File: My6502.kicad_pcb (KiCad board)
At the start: 2 copper layers, 99.7 x 99.7 mm, 38 parts, among them J1 ~NMI, J3 Power 5V, J4 Expansion Bus, J5 Port A, J6 Port B, SW1 RESET, U1 6502, U2 ROM 28C256, U3 RAM 62256, U4 74HCT00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

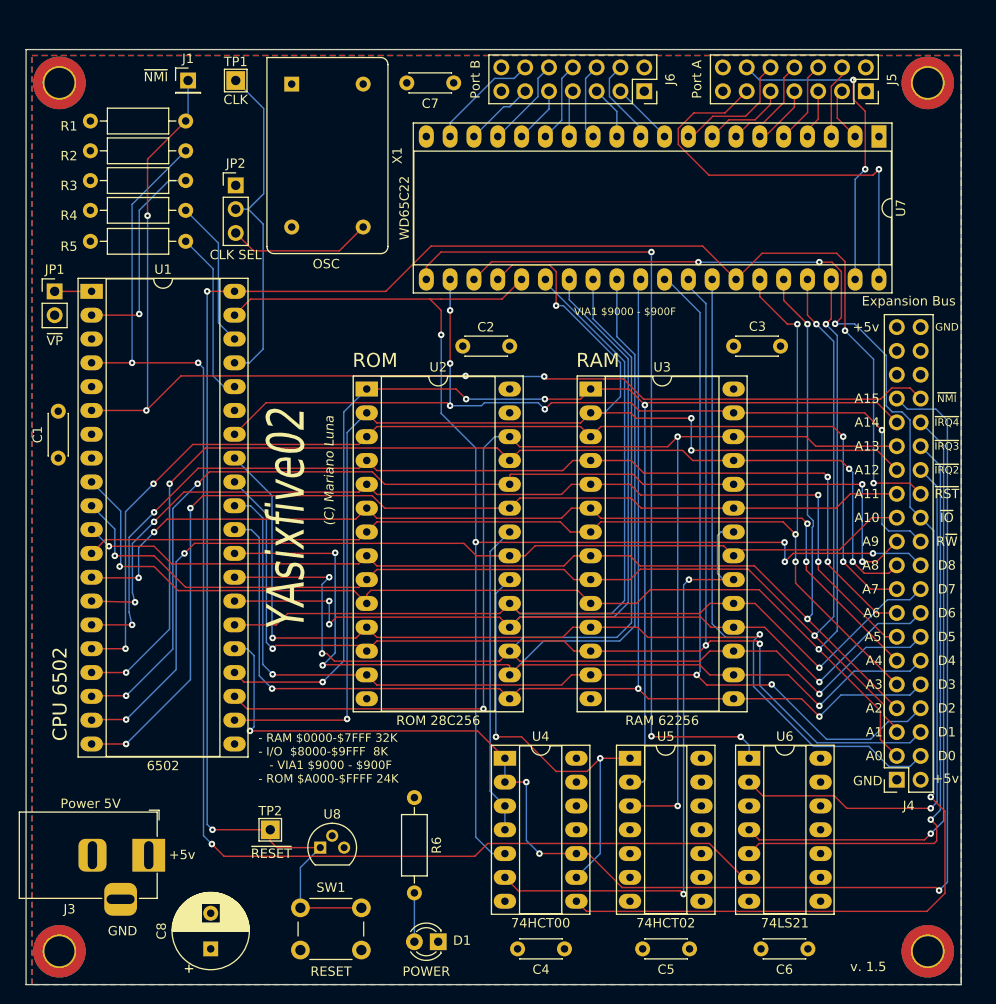
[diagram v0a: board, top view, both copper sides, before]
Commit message: Gerber file deleted had errors. New Schematic with power leads and GND Test
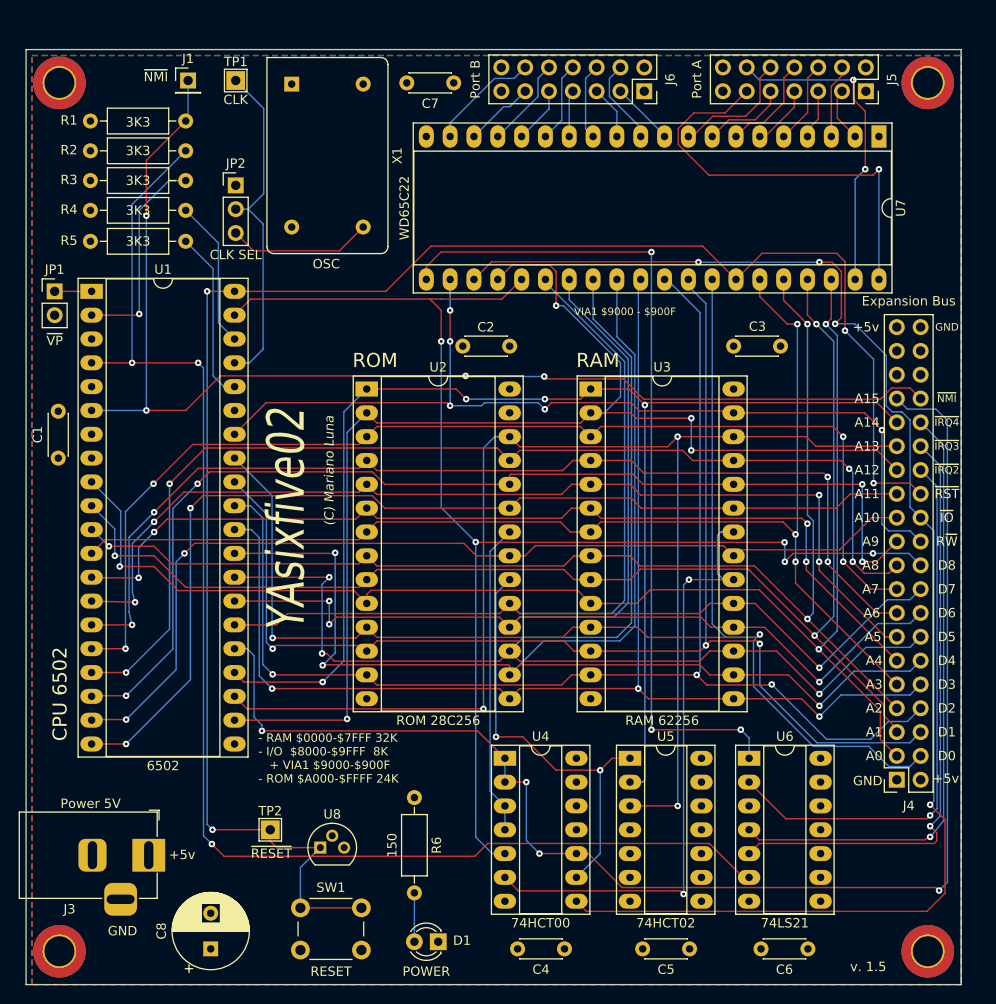
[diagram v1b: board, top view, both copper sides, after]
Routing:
- net ~ROM_CS: track 47.5 -> 46.2 mm
- net ~VIA2_IRQ: track 57.6 -> 58.9 mm
- net a15: track 153.1 -> 152.0 mm
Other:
- board text added: "- RAM $0000-$7FFF 32K - I/O $8000-$9FFF 8K + VIA1 $9000-$900F - ROM $A000-$FFFF 24K"
- board text removed: "- RAM $0000-$7FFF 32K - I/O $8000-$9FFF 8K - VIA1 $9000 - $900F - ROM $A000-$FFFF 24K"

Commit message: YAsicfive02 1.5 final version - Gerber file done
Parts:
- added J2: Aux 5VDC, Connector_PinHeader_2.54mm:PinHeader_1x03_P2.54mm_Vertical, F.Cu at (41.1, 146.2)
- added J7: GND, Connector_PinHeader_2.54mm:PinHeader_1x01_P2.54mm_Vertical, F.Cu at (122.2, 144.0)
- U1: value 6502 -> CPU 6502
- moved C8 5.80 mm to (53.8, 141.1), turned to 180 degrees
- moved J3 0.81 mm to (44.2, 135.3)
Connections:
- J3 pad 3: GND -> Net-(J2-Pad1)
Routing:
- net Net-(J2-Pad1): track 0.00 -> 11.9 mm

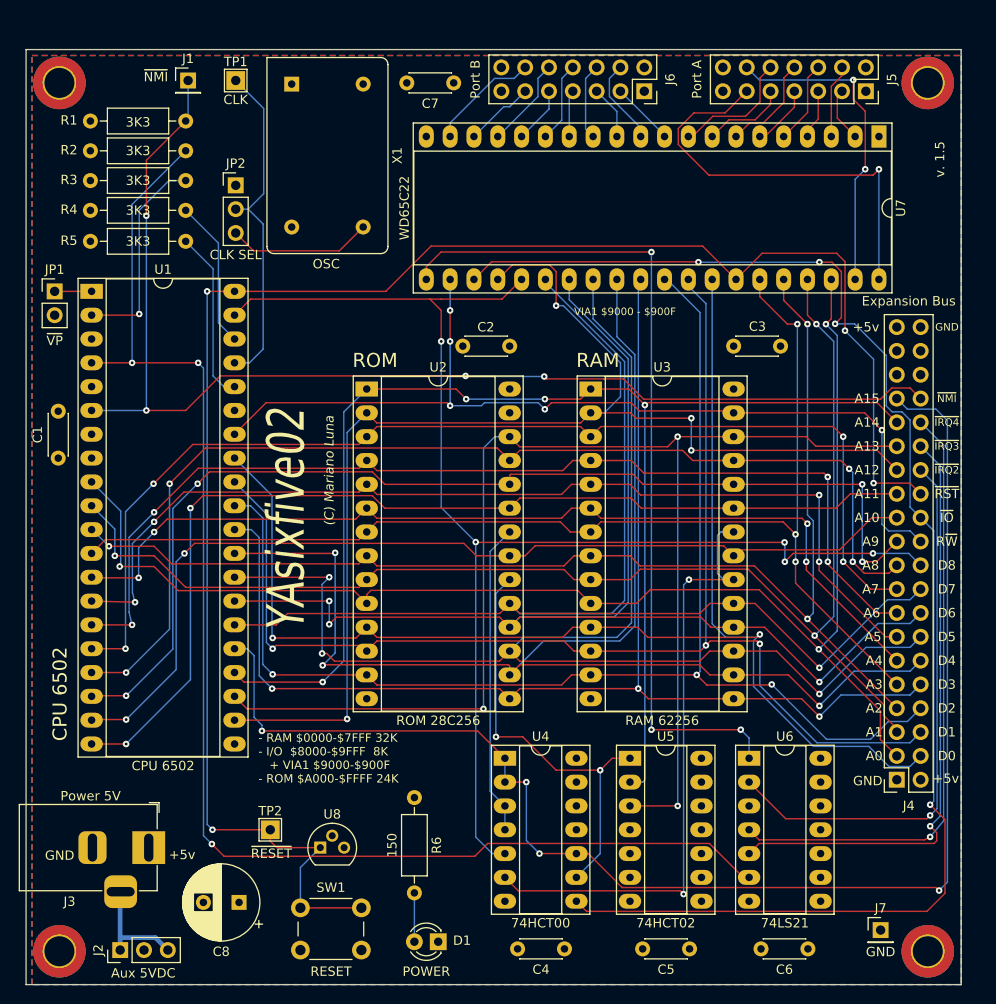
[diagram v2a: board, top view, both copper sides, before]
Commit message: PCB Component placement first take
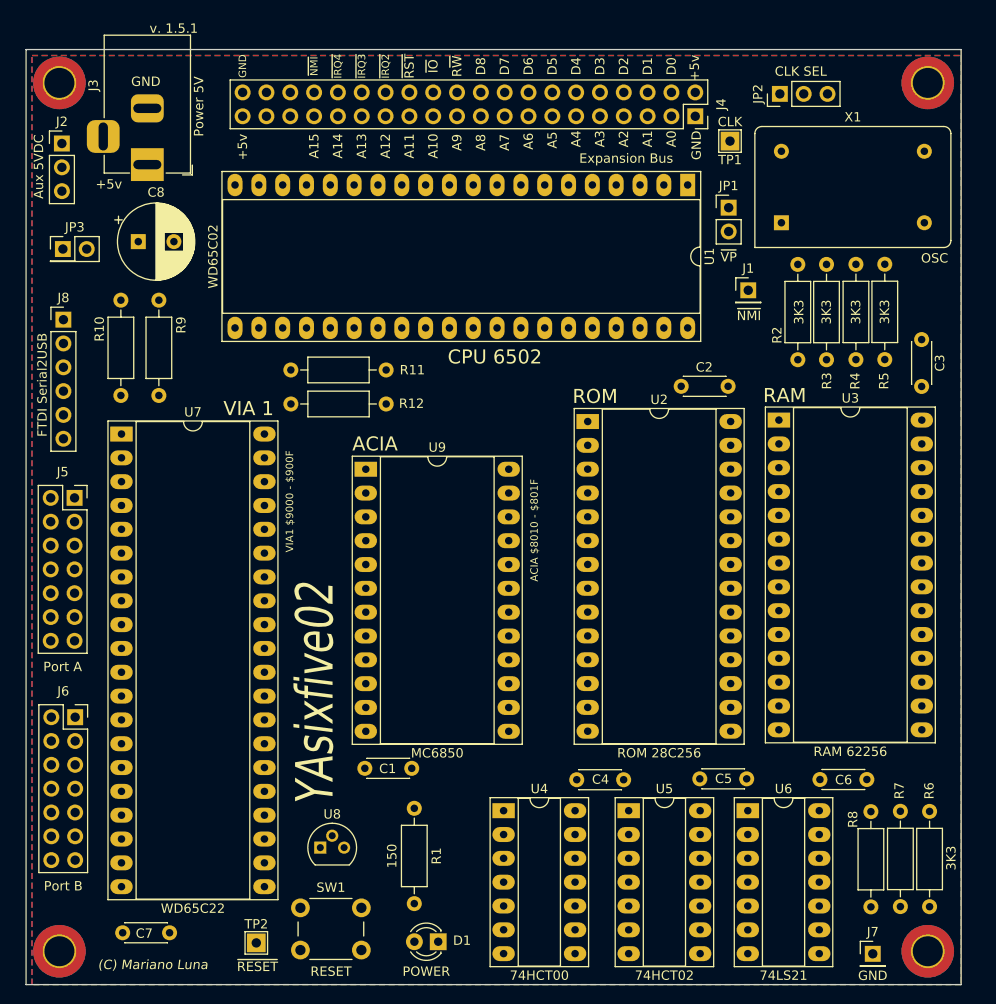
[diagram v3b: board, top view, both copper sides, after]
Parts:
- added J8: FTDI Serial2USB, Connector_PinHeader_2.54mm:PinHeader_1x06_P2.54mm_Vertical, F.Cu at (35.1, 79.0)
- added JP3: FTDI 5V, Connector_PinHeader_2.54mm:PinHeader_2x01_P2.54mm_Vertical, F.Cu at (35.0, 71.4)
- added R10: 2K7, Resistor_THT:R_Axial_DIN0207_L6.3mm_D2.5mm_P10.16mm_Horizontal, F.Cu at (41.2, 76.9)
- added R11: 2K7, Resistor_THT:R_Axial_DIN0207_L6.3mm_D2.5mm_P10.16mm_Horizontal, F.Cu at (69.5, 84.3)
- added R12: 2K7, Resistor_THT:R_Axial_DIN0207_L6.3mm_D2.5mm_P10.16mm_Horizontal, F.Cu at (59.3, 88.0)
- added R7: 3K3, Resistor_THT:R_Axial_DIN0207_L6.3mm_D2.5mm_P10.16mm_Horizontal, F.Cu at (124.3, 131.4)
- added R8: 3K3, Resistor_THT:R_Axial_DIN0207_L6.3mm_D2.5mm_P10.16mm_Horizontal, F.Cu at (121.2, 141.6)
- added R9: 2K7, Resistor_THT:R_Axial_DIN0207_L6.3mm_D2.5mm_P10.16mm_Horizontal, F.Cu at (45.3, 76.9)
- added U9: MC6850, Package_DIP:DIP-24_W15.24mm_Socket_LongPads, F.Cu at (67.3, 94.9)
- U1: value CPU 6502 -> WD65C02
- U8: value DS1813-10 -> DS1813
- moved R6 113.9 mm to (127.4, 131.4), turned to 270 degrees
- moved C7 97.2 mm to (41.4, 144.3), turned to 0 degrees
- moved J5 94.9 mm to (36.3, 98.0), turned to 0 degrees
- moved J6 90.2 mm to (36.3, 121.3), turned to 0 degrees
- moved U7 86.8 mm to (41.3, 91.2), turned to 0 degrees
- moved J2 86.2 mm to (34.9, 60.2), turned to 0 degrees
- moved R5 85.6 mm to (122.7, 83.2), turned to 90 degrees
- moved R4 83.2 mm to (119.6, 83.2), turned to 90 degrees
- moved R3 80.8 mm to (116.5, 83.2), turned to 90 degrees
- moved R2 79.6 mm to (113.4, 83.2), turned to 90 degrees
- moved J4 73.9 mm to (102.5, 57.3), turned to 270 degrees
- moved J3 72.8 mm to (44.0, 62.4), turned to 270 degrees
- moved JP1 72.4 mm to (106.0, 67.0)
- moved C8 71.3 mm to (43.1, 70.6), turned to 0 degrees
- moved U1 64.6 mm to (101.7, 64.6), turned to 270 degrees
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- renumbered R6 to R1, R1 to R2, R2 to R6
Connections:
- net Net-(J2-Pad1) renamed /Aux_0v
- J4 pad 32: ~ACIA_IRQ -> Net-(J4-Pad32)
- J4 pad 36: Net-(J4-Pad36) -> CLK
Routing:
- net ~RESET: track 187.8 -> 0.00 mm, vias 4 -> 0
- net ~IO_CS: track 154.5 -> 0.00 mm, vias 4 -> 0
- net a15: track 152.0 -> 0.00 mm, vias 4 -> 0
- net ~IRQ: track 148.1 -> 0.00 mm, vias 3 -> 0
- net a0: track 147.6 -> 0.00 mm, vias 3 -> 0
- net PHI2: track 145.8 -> 0.00 mm, vias 5 -> 0
- net d4: track 145.6 -> 0.00 mm, vias 3 -> 0
- net a13: track 145.3 -> 0.00 mm, vias 3 -> 0
- net d0: track 144.9 -> 0.00 mm, vias 2 -> 0
- net a14: track 143.7 -> 0.00 mm, vias 4 -> 0
- net d5: track 141.0 -> 0.00 mm, vias 3 -> 0
- net a1: track 140.9 -> 0.00 mm, vias 3 -> 0
- net d2: track 138.9 -> 0.00 mm, vias 3 -> 0
- net d1: track 137.7 -> 0.00 mm, vias 3 -> 0
- net d3: track 136.1 -> 0.00 mm, vias 3 -> 0
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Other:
- board text added: "ACIA"
- board text added: "ACIA $8010 - $801F"
- board text added: "VIA 1"
- board text added: "v. 1.5.1"
- board text removed: "v. 1.5"
